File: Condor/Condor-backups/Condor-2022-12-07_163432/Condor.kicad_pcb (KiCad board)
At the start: 2 copper layers, 40 x 40 mm, 6 parts

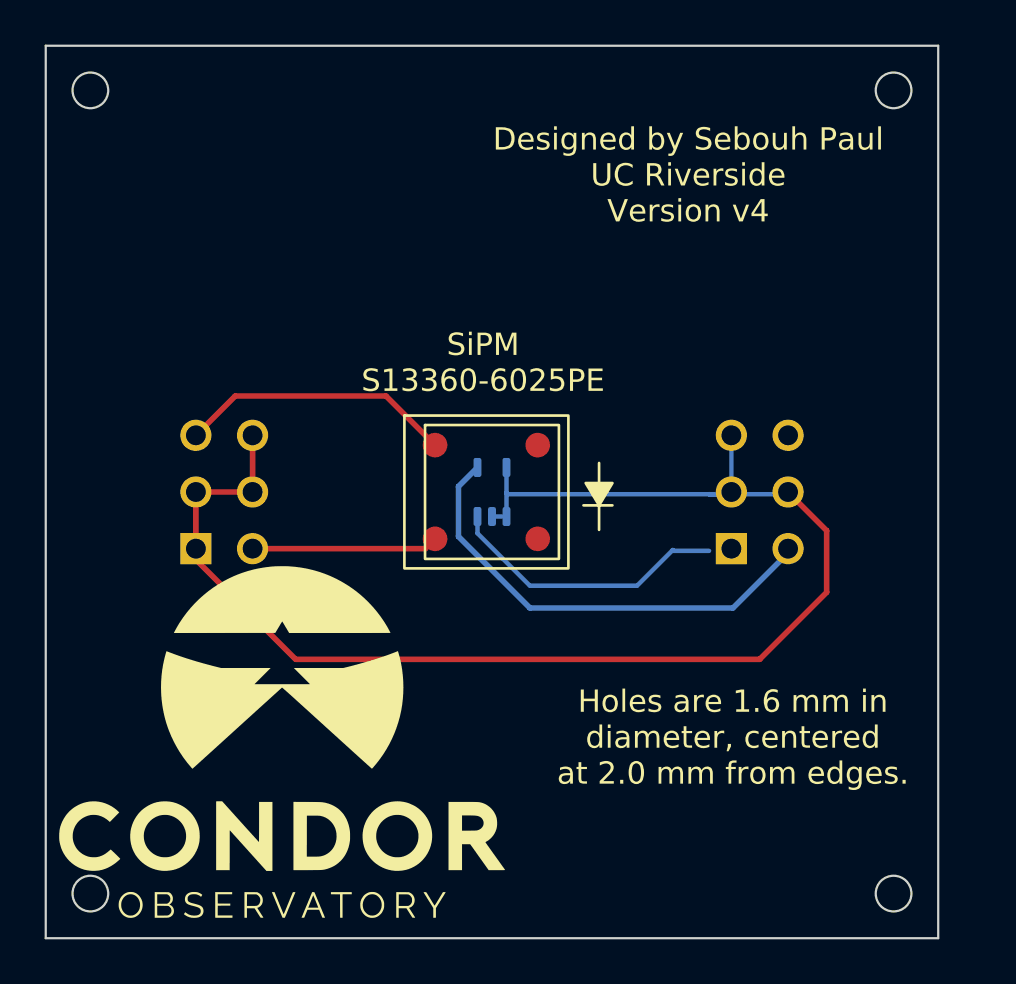
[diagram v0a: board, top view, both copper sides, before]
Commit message: updated condor board.  v4:  added a notch to indicate the polarity of the connector
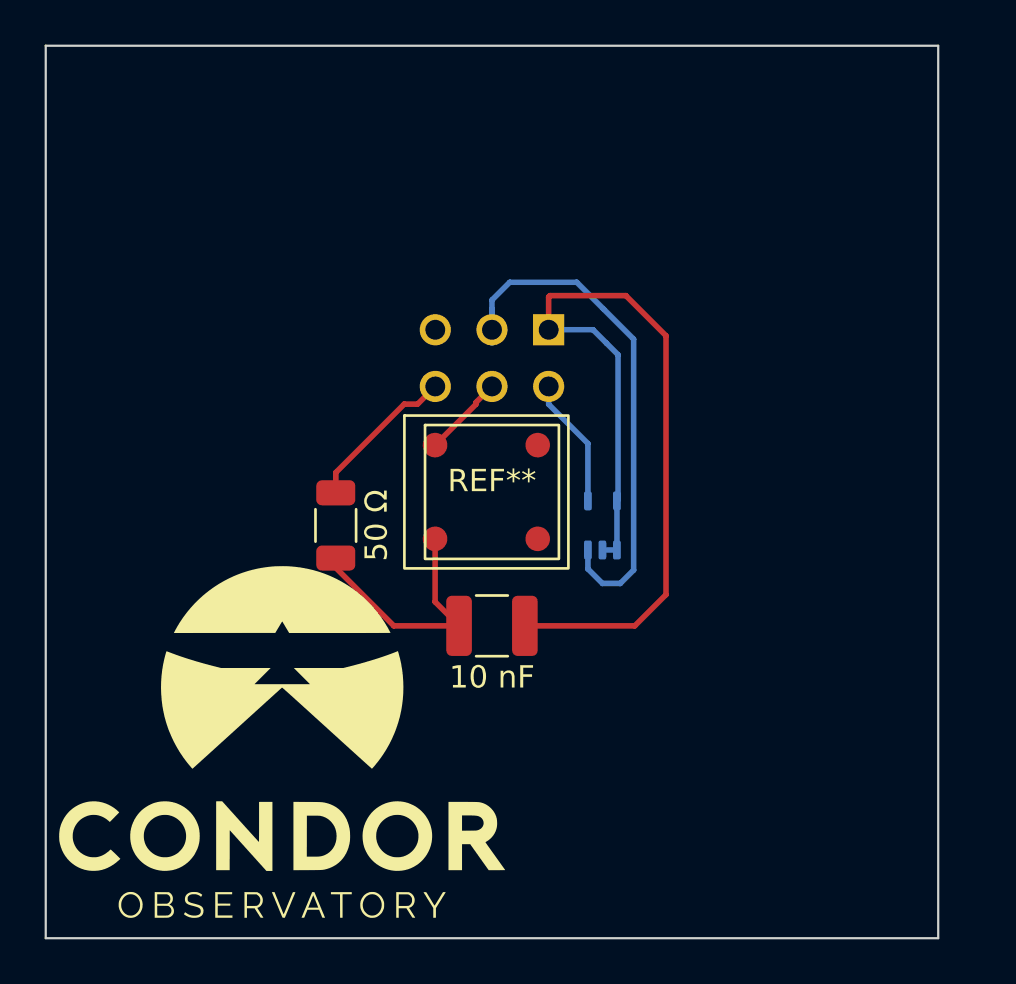
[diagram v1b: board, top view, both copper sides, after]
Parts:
- removed the REF** at (179.8, 100.2)
- removed the REF** at (187.0, 100.0)
- added 10 nF: C_1210_3225Metric, Capacitor_SMD:C_1210_3225Metric, F.Cu at (175.0, 106.0)
- added 50 Ω: R_1206_3216Metric, Resistor_SMD:R_1206_3216Metric, F.Cu at (168.0, 101.5)
- moved REF** 13.4 mm to (175.0, 94.0), turned to 180 degrees
- moved REF** 5.17 mm to (179.9, 101.5)
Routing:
- net (no net): track 118.0 -> 90.8 mm
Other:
- outline, holes or cut-outs redrawn
- board text removed: "ANODE"
- board text removed: "CATHODE"
- board text removed: "Connector for SiPM"
- board text removed: "Connector for temp sensor"
- board text removed: "Designed by Sebouh Paul UC Riverside Version v4"
- board text removed: "GND"
- board text removed: "Holes are 1.6 mm in diameter, centered at 2.0 mm from edges."
- board text removed: "OUT"
- board text removed: "SiPM S13360-6025PE"
- board text removed: "Temp Sensor LM94021QBIMG/NOPB"
- board text removed: "VDD"
